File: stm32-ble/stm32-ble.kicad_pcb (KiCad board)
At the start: 4 copper layers, 42 parts, among them J1 USB_C_Receptacle_USB2.0, J2 TC2030, J3 Conn_01x04, J4 Conn_Coaxial, SW1 SW_Push, U1 USBLC6-2SC6, U2 MIC5365-3.3YD5, U3 STM32WB35CEU6A, X1 32khz768, X2 32MHz

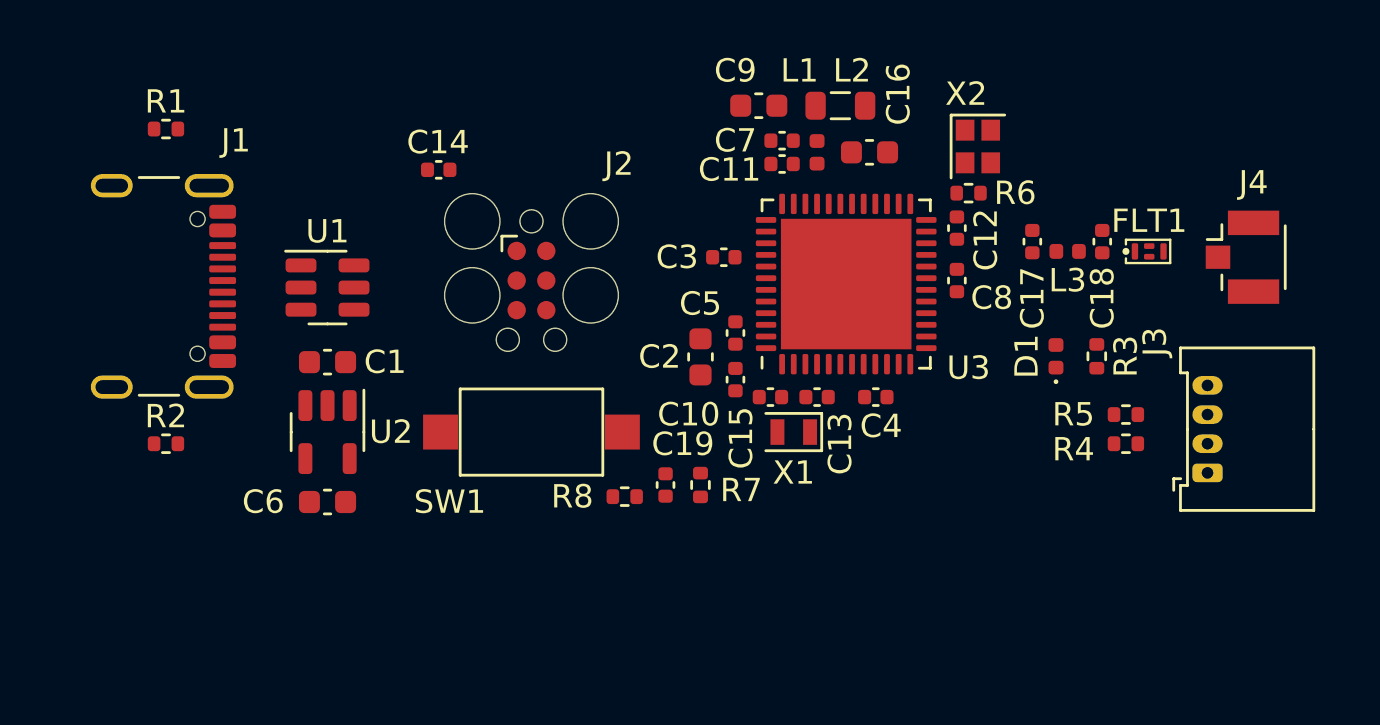
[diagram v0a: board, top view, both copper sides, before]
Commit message: fiducials, mounting holes and preliminary via placement
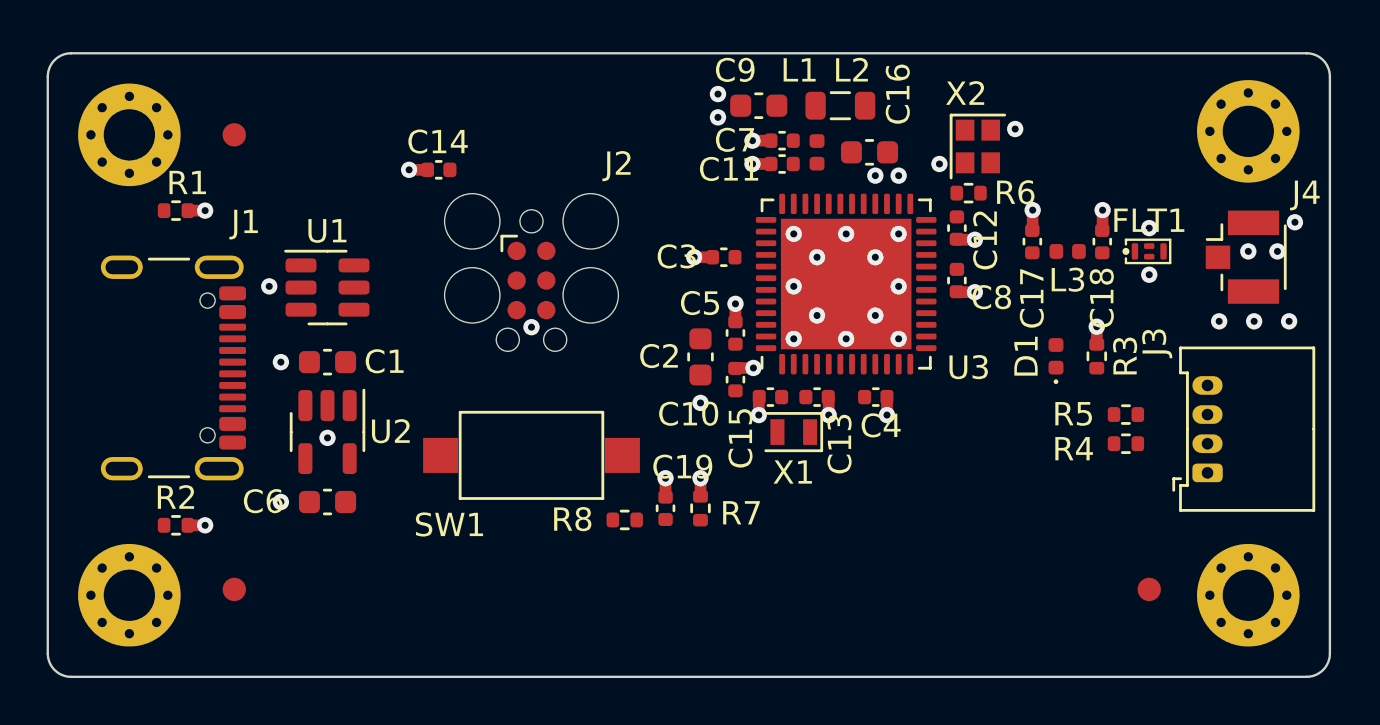
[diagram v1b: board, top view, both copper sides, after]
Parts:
- added FM1: Fiducial, Fiducial:Fiducial_1mm_Mask2mm, F.Cu at (99.0, 88.5)
- added FM2: Fiducial, Fiducial:Fiducial_1mm_Mask2mm, F.Cu at (99.0, 108.0)
- added FM3: Fiducial, Fiducial:Fiducial_1mm_Mask2mm, F.Cu at (138.2, 108.0)
- added H1: MountingHole_Pad, MountingHole:MountingHole_2.2mm_M2_Pad_Via, F.Cu at (94.5, 88.5)
- added H2: MountingHole_Pad, MountingHole:MountingHole_2.2mm_M2_Pad_Via, F.Cu at (142.5, 88.3)
- added H3: MountingHole_Pad, MountingHole:MountingHole_2.2mm_M2_Pad_Via, F.Cu at (142.5, 108.2)
- added H4: MountingHole_Pad, MountingHole:MountingHole_2.2mm_M2_Pad_Via, F.Cu at (94.5, 108.2)
- moved J1 3.53 mm to (95.2, 98.5)
- moved R1 3.53 mm to (96.5, 91.8)
- moved R2 3.53 mm to (96.5, 105.2)
- moved C19 1.00 mm to (117.5, 104.5)
- moved R7 1.00 mm to (119.0, 104.5)
- moved R8 1.00 mm to (115.8, 105.0)
- moved SW1 1.00 mm to (111.8, 102.2)
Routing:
- net GND: track 0.00 -> 13.8 mm, vias 0 -> 50
- added copper zone on In1.Cu, net GND
- added copper zone on In2.Cu, net GND
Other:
- board outline added: 55 x 26.8 mm

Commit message: drc
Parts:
- moved C14 23.1 mm to (126.5, 103.4), turned to 0 degrees
- moved R2 13.4 mm to (97.7, 91.9)
- moved R1 13.2 mm to (97.7, 104.9)
- moved C9 1.75 mm to (121.5, 89.0)
- moved C15 1.63 mm to (121.5, 101.3)
- moved C10 1.58 mm to (120.0, 100.5)
- moved C2 1.58 mm to (118.5, 99.5)
- moved C5 1.58 mm to (120.0, 98.5)
- moved C13 1.55 mm to (124.0, 101.3)
- moved C8 1.53 mm to (130.3, 96.2)
- moved X1 1.52 mm to (122.8, 102.8)
- moved C4 1.52 mm to (126.8, 101.2)
- moved C11 1.52 mm to (122.5, 91.3)
- moved C7 1.52 mm to (122.5, 90.3)
- moved L1 1.52 mm to (124.0, 90.8)
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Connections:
- net Net-(U3-PC14) renamed /LSE_IN
- net Net-(U3-PC15) renamed /LSE_OUT
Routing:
- net /SWD_NRST: track 0.00 -> 38.2 mm
- net +5V: track 0.00 -> 26.3 mm
- net +3.3V: track 0.00 -> 22.3 mm, vias 0 -> 14
- net /USB_D+: track 0.00 -> 21.8 mm
- net /USB_D-: track 0.00 -> 21.8 mm
- net /BOOT0: track 0.00 -> 13.5 mm
- net /SWD_DIO: track 0.00 -> 12.8 mm
- net /UART_TX: track 0.00 -> 10.5 mm
- net /SWD_CLK: track 0.00 -> 9.75 mm
- net /SWD_TRC: track 0.00 -> 9.54 mm
- net /UART_RX: track 0.00 -> 9.47 mm
- net /USBC_D-: track 0.00 -> 9.40 mm
- net Net-(R8-Pad2): track 0.00 -> 8.64 mm
- net /USBC_D+: track 0.00 -> 7.34 mm
- net /USBC_CC1: track 0.00 -> 7.28 mm
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- added copper zone on B.Cu, net +3.3V
- added copper zone on F.Cu, net +3.3V
- added copper zone on F.Cu, net GND
